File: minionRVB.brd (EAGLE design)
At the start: 100.3 x 100 mm, 119 parts, among them IC1 74HCT245DW

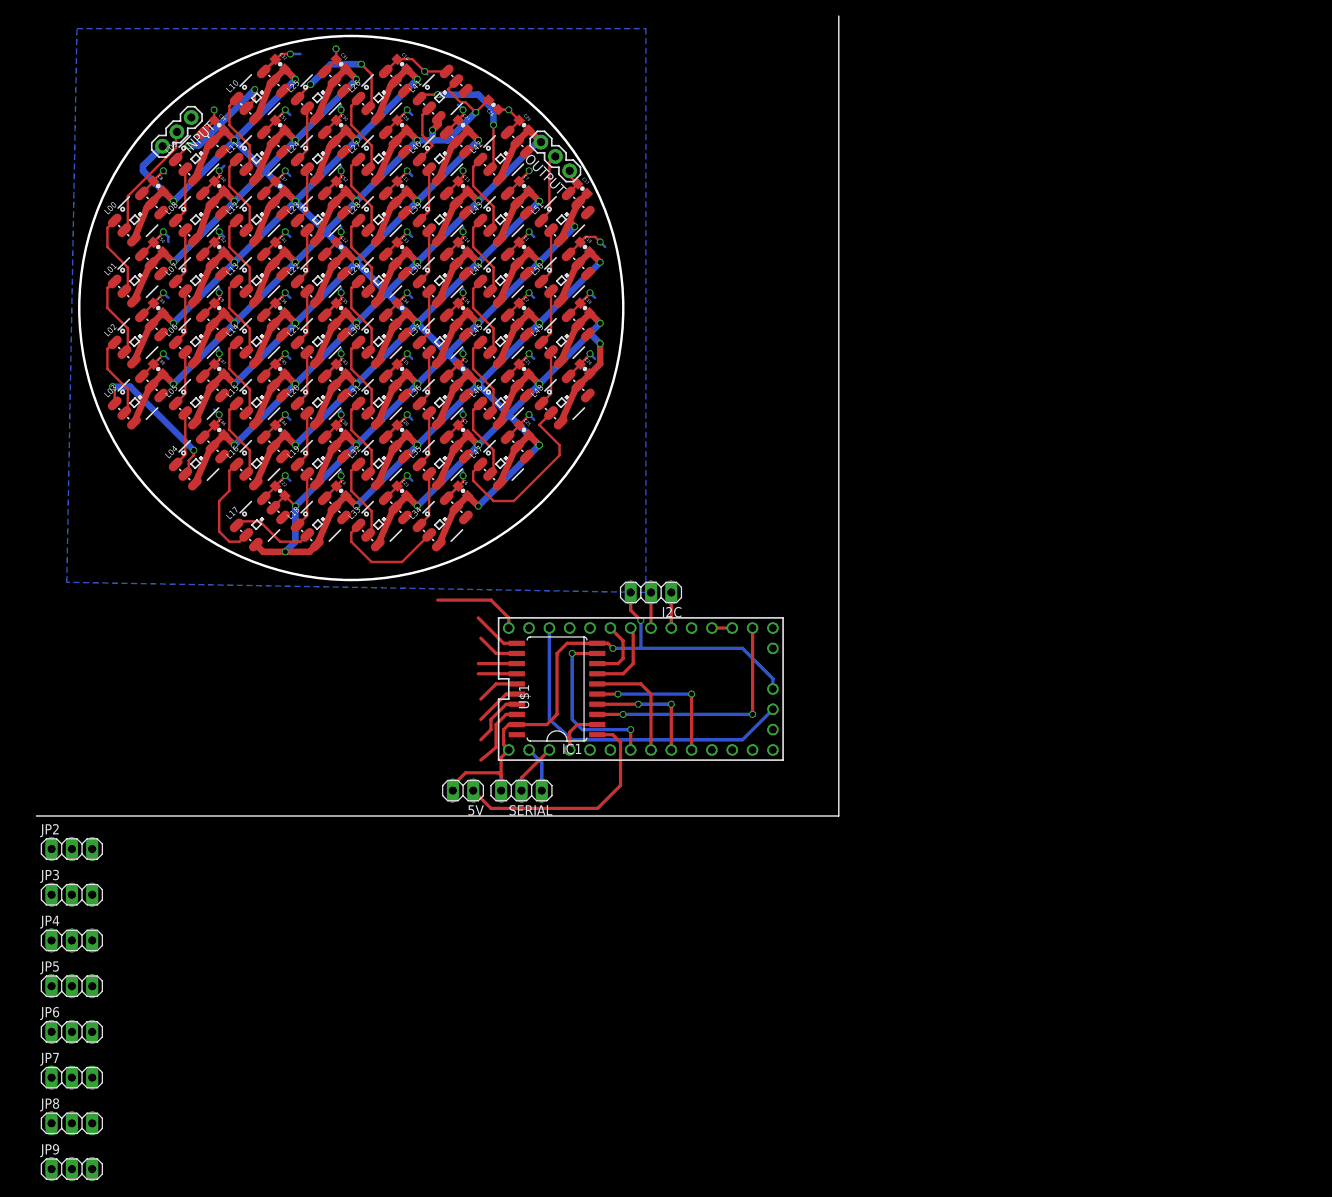
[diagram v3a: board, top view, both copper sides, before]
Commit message: Teensy adaptor v3
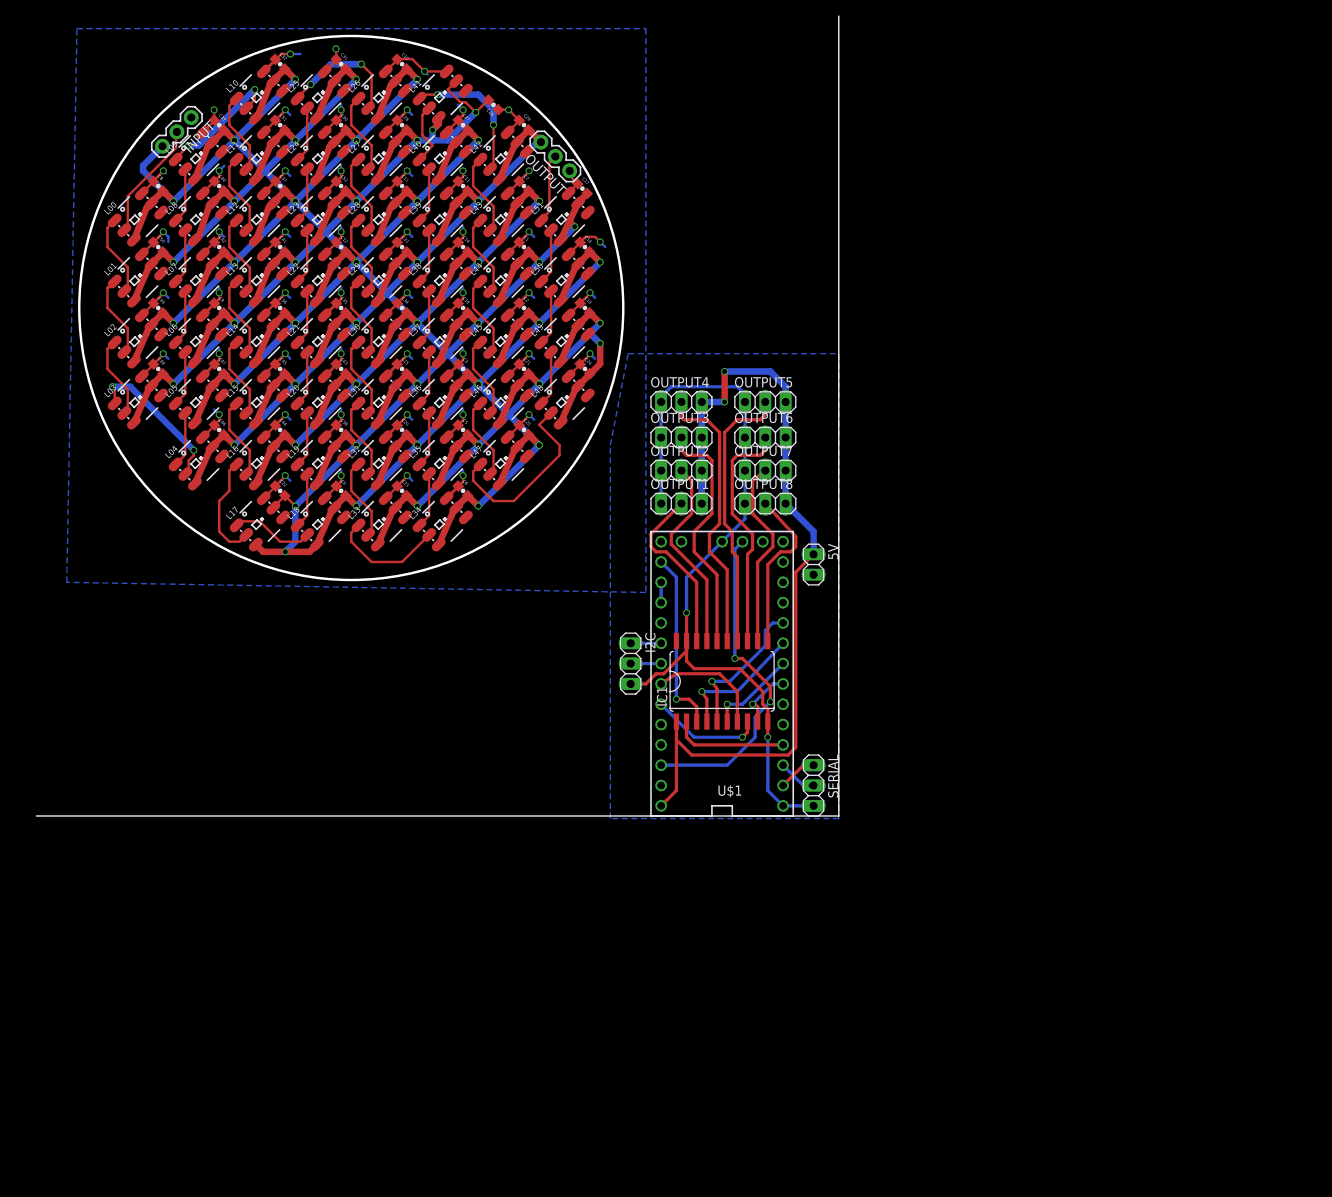
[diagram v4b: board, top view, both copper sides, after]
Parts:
- removed JP2, JP3, JP4, JP5, JP6, JP7, JP8, JP9: (no value), pinhead:1X03
- added OUTPUT1, OUTPUT2, OUTPUT3, OUTPUT4, OUTPUT5, OUTPUT6, OUTPUT7, OUTPUT8: (no value), pinhead:1X03
- moved 5V 52.1 mm to (97.2, 31.4), turned to 270 degrees
- moved SERIAL 36.5 mm to (97.2, 3.81), turned to 270 degrees
- moved IC1 20.7 mm to (85.7, 16.8), turned to 0 degrees
- moved U$1 10.3 mm to (85.7, 17.8), turned to 180 degrees
- moved I2C 9.25 mm to (74.3, 19.1), turned to 270 degrees
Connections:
- net 5V: now also OUTPUT1.3, OUTPUT2.3, OUTPUT3.3, OUTPUT4.3, OUTPUT5.3, OUTPUT6.3, OUTPUT7.3, OUTPUT8.3; no longer JP2.3, JP3.3, JP4.3, JP5.3, JP6.3, JP7.3, JP8.3, JP9.3
- net GND: now also OUTPUT1.1, OUTPUT2.1, OUTPUT3.1, OUTPUT4.1, OUTPUT5.1, OUTPUT6.1, OUTPUT7.1, OUTPUT8.1; no longer JP2.1, JP3.1, JP4.1, JP5.1, JP6.1, JP7.1, JP8.1, JP9.1
- net N$42: now also OUTPUT1.2; no longer JP2.2
- net N$54: now also OUTPUT2.2; no longer JP3.2
- net N$55: now also OUTPUT3.2; no longer JP4.2
- net N$56: now also OUTPUT4.2; no longer JP5.2
- net N$57: now also OUTPUT5.2; no longer JP6.2
- net N$58: now also OUTPUT6.2; no longer JP7.2
- net N$59: now also OUTPUT7.2; no longer JP8.2
- net N$60: now also OUTPUT8.2; no longer JP9.2
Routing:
- net 5V: track 40.3 -> 102.7 mm, vias 0 -> 2
- net GND: track 332.5 -> 364.8 mm
- net N$56: track 5.28 -> 35.0 mm
- net N$57: track 4.81 -> 34.3 mm
- net N$58: track 4.81 -> 30.1 mm
- net N$55: track 5.81 -> 30.6 mm
- net N$59: track 5.28 -> 23.9 mm
- net N$54: track 7.08 -> 24.7 mm
- net N$60: track 6.13 -> 20.9 mm
- net STRIP08: track 21.7 -> 7.48 mm, vias 2 -> 1
- net N$42: track 8.45 -> 21.9 mm
- net STRIP01: track 6.06 -> 14.4 mm
- net STRIP02: track 30.2 -> 22.7 mm, vias 2 -> 1
- net STRIP07: track 7.96 -> 14.1 mm, vias 0 -> 1
- net STRIP06: track 9.60 -> 14.6 mm
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
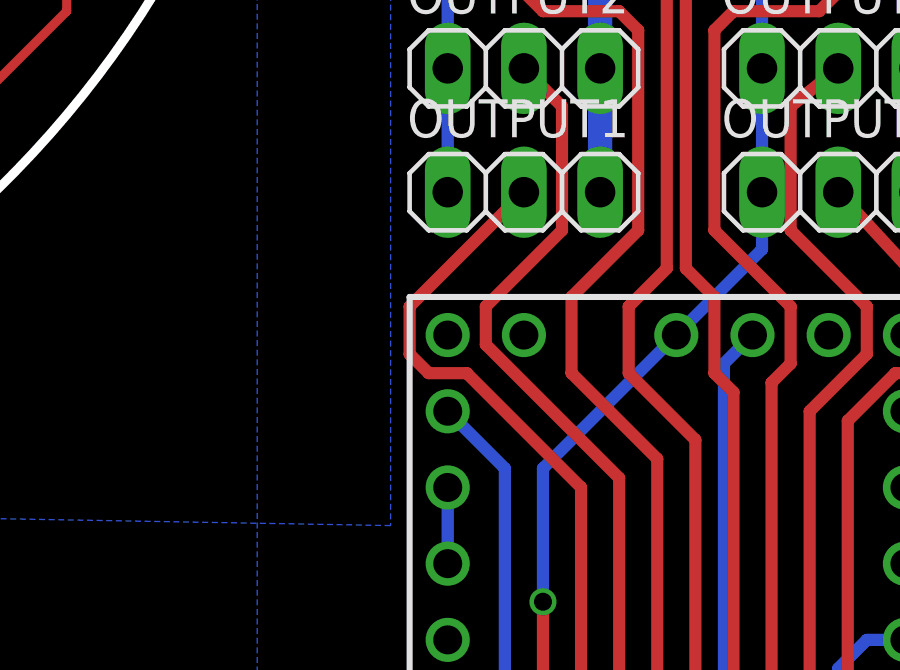
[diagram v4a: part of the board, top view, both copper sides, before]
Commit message: Add an optional second alim
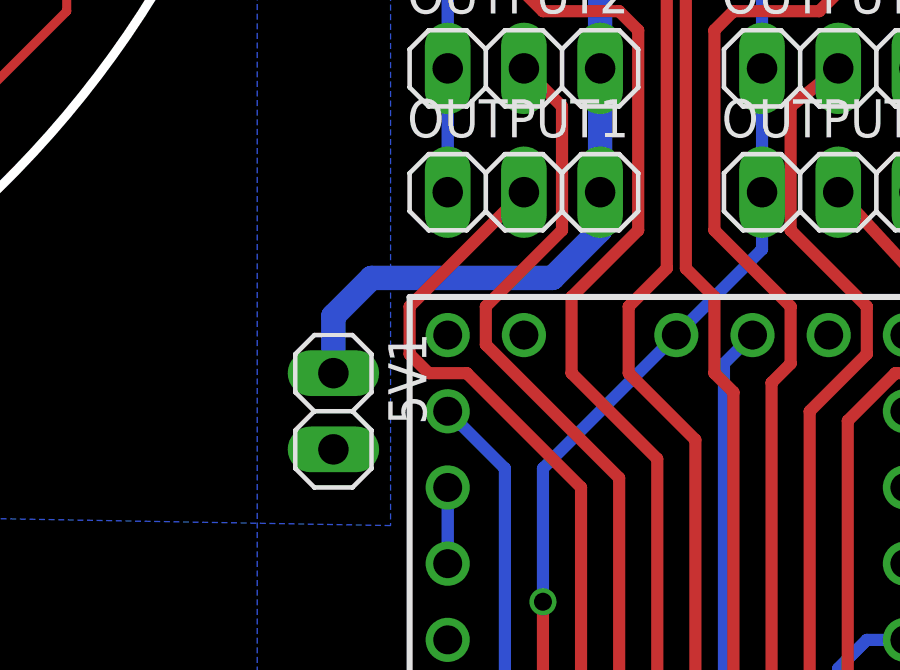
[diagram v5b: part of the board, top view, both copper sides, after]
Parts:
- added 5V1: (no value), pinhead:1X02
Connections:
- net 5V: now also 5V1.1
- net GND: now also 5V1.2
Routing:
- net 5V: track 102.7 -> 115.9 mm
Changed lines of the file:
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@@
 <element name="OUTPUT7" library="pinhead" package="1X03" value="" x="91.1225" y="43.18"/>
 <element name="OUTPUT8" library="pinhead" package="1X03" value="" x="91.1225" y="39.0525"/>
+<element name="5V1" library="pinhead" package="1X02" value="" x="74.295" y="31.75" rot="R270"/>
 </elements>
 <signals>
@@
 <vertex x="71.755" y="46.355"/>
 </polygon>
+<contactref element="5V1" pad="2"/>
 <wire x1="69.85" y1="57.15" x2="78.105" y2="52.3875" width="0" layer="19" extent="16-16"/>
 </signal>
@@
 <wire x1="94.9325" y1="8.5725" x2="94.9325" y2="30.48" width="0.4064" layer="1"/>
 <wire x1="94.9325" y1="30.48" x2="97.155" y2="32.7025" width="0.4064" layer="1"/>
+<contactref element="5V1" pad="1"/>
+<wire x1="74.295" y1="33.02" x2="74.295" y2="34.925" width="0.8128" layer="16"/>
+<wire x1="74.295" y1="34.925" x2="75.565" y2="36.195" width="0.8128" layer="16"/>
+<wire x1="75.565" y1="36.195" x2="81.5975" y2="36.195" width="0.8128" layer="16"/>
+<wire x1="81.5975" y1="36.195" x2="83.185" y2="37.7825" width="0.8128" layer="16"/>
+<wire x1="83.185" y1="37.7825" x2="83.185" y2="39.0525" width="0.8128" layer="16"/>
 </signal>
 </signals>

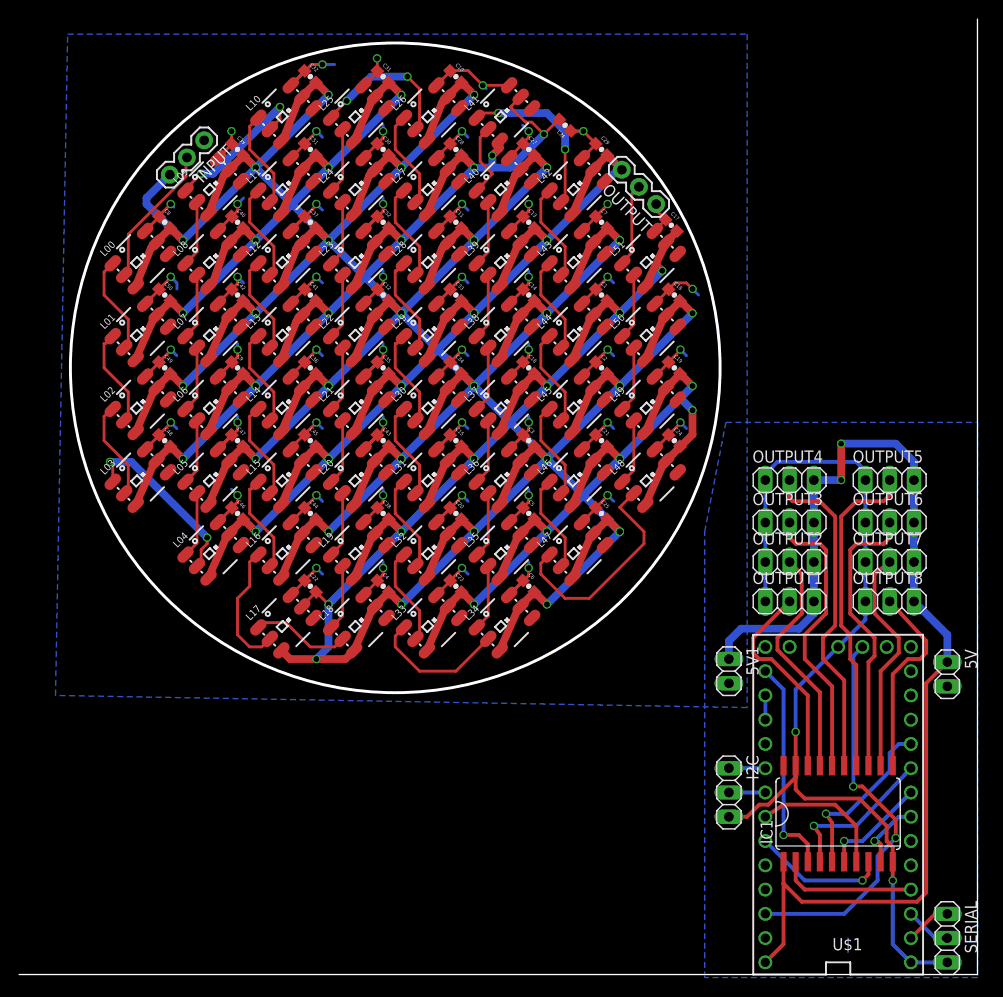
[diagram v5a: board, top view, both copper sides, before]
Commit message: Pinswap 5v - signal + DRU OK
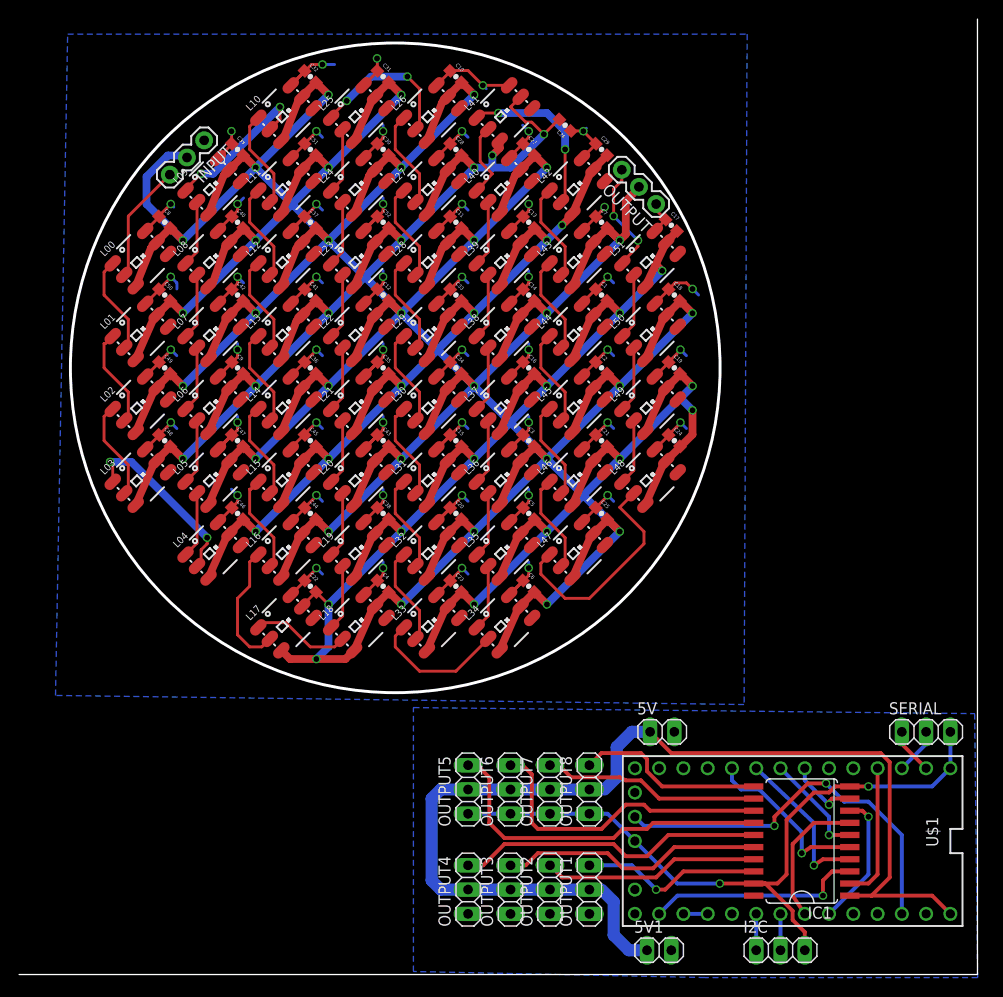
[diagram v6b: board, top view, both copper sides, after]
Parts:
- moved OUTPUT5 54.7 mm to (47.0, 19.4), turned to 90 degrees
- moved OUTPUT4 54.5 mm to (47.0, 8.89), turned to 90 degrees
- moved OUTPUT6 48.5 mm to (51.4, 19.4), turned to 90 degrees
- moved OUTPUT3 48.3 mm to (51.4, 8.89), turned to 90 degrees
- moved OUTPUT7 42.8 mm to (55.6, 19.4), turned to 90 degrees
- moved OUTPUT2 42.5 mm to (55.6, 8.89), turned to 90 degrees
- moved OUTPUT8 37.1 mm to (59.7, 19.4), turned to 90 degrees
- moved OUTPUT1 36.7 mm to (59.7, 8.89), turned to 90 degrees
- moved 5V 30.4 mm to (67.3, 25.4), turned to 0 degrees
- moved 5V1 30.1 mm to (67.0, 2.54), turned to 0 degrees
- moved SERIAL 21.7 mm to (94.9, 25.4), turned to 0 degrees
- moved I2C 17.4 mm to (79.7, 2.54), turned to 0 degrees
- moved U$1 6.10 mm to (81.0, 14.0), turned to 270 degrees
- moved IC1 4.76 mm to (81.9, 14.0), turned to 90 degrees
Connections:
- net 5V: now also OUTPUT1.2, OUTPUT2.2, OUTPUT3.2, OUTPUT4.2, OUTPUT5.2, OUTPUT6.2, OUTPUT7.2, OUTPUT8.2; no longer OUTPUT1.3, OUTPUT2.3, OUTPUT3.3, OUTPUT4.3, OUTPUT5.3, OUTPUT6.3, OUTPUT7.3, OUTPUT8.3
- net DI: now also INPUT.3; no longer INPUT.2
- net DOUT: now also OUTPUT.3; no longer OUTPUT.2
- net N$42: now also OUTPUT1.3; no longer OUTPUT1.2
- net N$54: now also OUTPUT2.3; no longer OUTPUT2.2
- net N$55: now also OUTPUT3.3; no longer OUTPUT3.2
- net N$56: now also OUTPUT4.3; no longer OUTPUT4.2
- net N$57: now also OUTPUT5.3; no longer OUTPUT5.2
- net N$58: now also OUTPUT6.3; no longer OUTPUT6.2
- net N$59: now also OUTPUT7.3; no longer OUTPUT7.2
- net N$60: now also OUTPUT8.3; no longer OUTPUT8.2
- net VCC: now also INPUT.2, OUTPUT.2; no longer INPUT.3, OUTPUT.3
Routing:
- net GND: track 364.8 -> 338.4 mm
- net DOUT: track 8.73 -> 11.9 mm, vias 0 -> 2
- net N$55: track 30.6 -> 27.6 mm
- net VCC: track 976.0 -> 979.0 mm, vias 78 -> 54
- net N$42: track 21.9 -> 19.0 mm, vias 0 -> 1
- net N$56: track 35.0 -> 32.3 mm
- net DI: track 15.0 -> 12.5 mm
- net N$58: track 30.1 -> 32.5 mm
- net N$57: track 34.3 -> 36.5 mm
- net N$54: track 24.7 -> 22.6 mm
- net N$59: track 23.9 -> 22.7 mm
- net N$60: track 20.9 -> 19.9 mm
- net 5V: track 115.9 -> 116.3 mm, vias 2 -> 0
- net TX: vias 1 -> 0

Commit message: Condo party!!!! \o/
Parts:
- added C53, C54, C55, C56, C57, C58, C59, C60: 0.1uF, SparkFun:0603-CAP
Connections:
- net GND: now also C53.1, C54.1, C55.1, C56.1, C57.1, C58.1, C59.1, C60.1
- net VCC: now also C53.2, C54.2, C55.2, C56.2, C57.2, C58.2, C59.2, C60.2
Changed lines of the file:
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@@
 <element name="OUTPUT8" library="pinhead" package="1X03" value="" x="59.69" y="19.3675" rot="R90"/>
 <element name="5V1" library="pinhead" package="1X02" value="" x="66.9925" y="2.54"/>
+<element name="C53" library="SparkFun" package="0603-CAP" value="0.1uF" x="1.5875" y="-6.6675"/>
+<element name="C54" library="SparkFun" package="0603-CAP" value="0.1uF" x="1.5875" y="-9.8425"/>
+<element name="C55" library="SparkFun" package="0603-CAP" value="0.1uF" x="1.5875" y="-13.0175"/>
+<element name="C56" library="SparkFun" package="0603-CAP" value="0.1uF" x="1.5875" y="-16.1925"/>
+<element name="C57" library="SparkFun" package="0603-CAP" value="0.1uF" x="1.5875" y="-19.3675"/>
+<element name="C58" library="SparkFun" package="0603-CAP" value="0.1uF" x="4.7625" y="-19.3675"/>
+<element name="C59" library="SparkFun" package="0603-CAP" value="0.1uF" x="1.5875" y="-22.5425"/>
+<element name="C60" library="SparkFun" package="0603-CAP" value="0.1uF" x="4.7625" y="-22.5425"/>
 </elements>
 <signals>
@@
 <wire x1="62.865" y1="76.835" x2="63.5" y2="77.47" width="0.8128" layer="1"/>
 <wire x1="63.5" y1="77.47" x2="63.5" y2="80.9625" width="0.8128" layer="1"/>
+<contactref element="C54" pad="2"/>
+<contactref element="C55" pad="2"/>
+<contactref element="C58" pad="2"/>
+<contactref element="C60" pad="2"/>
+<contactref element="C53" pad="2"/>
+<contactref element="C59" pad="2"/>
+<contactref element="C56" pad="2"/>
+<contactref element="C57" pad="2"/>
 <wire x1="50.305025" y1="33.930859375" x2="76.8858" y2="8.255" width="0" layer="19" extent="1-1"/>
+<wire x1="2.4375" y1="-6.6675" x2="28.355884375" y2="33.02" width="0" layer="19" extent="1-1"/>
+<wire x1="2.4375" y1="-9.8425" x2="2.4375" y2="-6.6675" width="0" layer="19" extent="1-1"/>
+<wire x1="2.4375" y1="-13.0175" x2="2.4375" y2="-9.8425" width="0" layer="19" extent="1-1"/>
+<wire x1="2.4375" y1="-16.1925" x2="2.4375" y2="-13.0175" width="0" layer="19" extent="1-1"/>
+<wire x1="2.4375" y1="-19.3675" x2="2.4375" y2="-16.1925" width="0" layer="19" extent="1-1"/>
+<wire x1="2.4375" y1="-22.5425" x2="2.4375" y2="-19.3675" width="0" layer="19" extent="1-1"/>
+<wire x1="5.6125" y1="-22.5425" x2="2.4375" y2="-22.5425" width="0" layer="19" extent="1-1"/>
+<wire x1="5.6125" y1="-19.3675" x2="2.4375" y2="-19.3675" width="0" layer="19" extent="1-1"/>
 </signal>
 <signal name="GND">
@@
 </polygon>
 <contactref element="5V1" pad="2"/>
+<contactref element="C54" pad="1"/>
+<contactref element="C55" pad="1"/>
+<contactref element="C58" pad="1"/>
+<contactref element="C53" pad="1"/>
+<contactref element="C57" pad="1"/>
+<contactref element="C60" pad="1"/>
+<contactref element="C59" pad="1"/>
+<contactref element="C56" pad="1"/>
+<wire x1="0.7375" y1="-19.3675" x2="0.7375" y2="-22.5425" width="0" layer="19" extent="1-1"/>
+<wire x1="3.9125" y1="-22.5425" x2="0.7375" y2="-22.5425" width="0" layer="19" extent="1-1"/>
+<wire x1="3.9125" y1="-19.3675" x2="0.7375" y2="-19.3675" width="0" layer="19" extent="1-1"/>
+<wire x1="0.7375" y1="-16.1925" x2="0.7375" y2="-19.3675" width="0" layer="19" extent="1-1"/>
+<wire x1="0.7375" y1="-13.0175" x2="0.7375" y2="-16.1925" width="0" layer="19" extent="1-1"/>
+<wire x1="0.7375" y1="-9.8425" x2="0.7375" y2="-13.0175" width="0" layer="19" extent="1-1"/>
+<wire x1="0.7375" y1="-6.6675" x2="0.7375" y2="-9.8425" width="0" layer="19" extent="1-1"/>
+<wire x1="46.355" y1="6.35" x2="0.7375" y2="-6.6675" width="0" layer="19" extent="1-16"/>
 <wire x1="53.34" y1="41.774165625" x2="68.58" y2="25.4" width="0" layer="19" extent="1-1"/>
 </signal>
